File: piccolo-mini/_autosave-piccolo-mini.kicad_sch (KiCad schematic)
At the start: 13 parts, among them U1 ProMicro

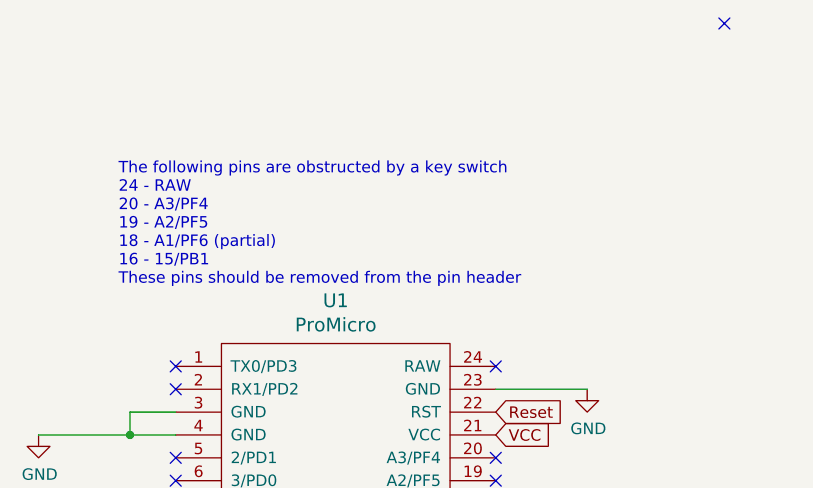
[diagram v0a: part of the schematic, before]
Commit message: Remove a few pro micro pins that get in the way
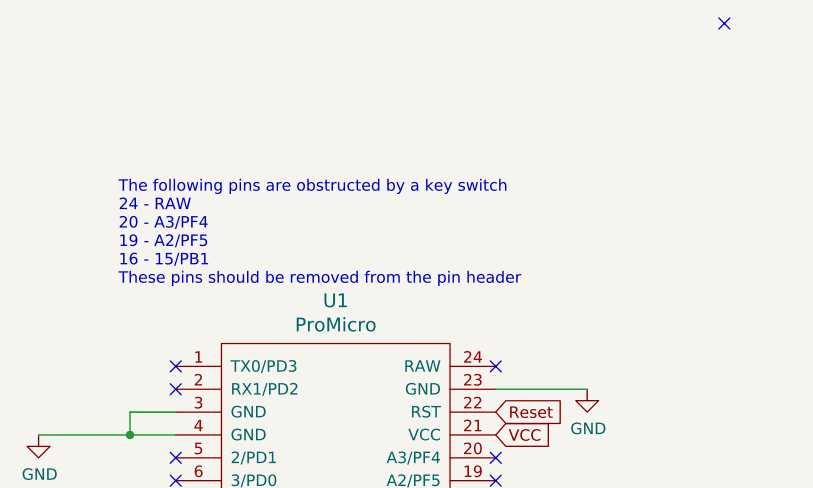
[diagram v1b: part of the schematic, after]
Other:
- note added: "The following pins are obstructed by a key switch 24 - RAW 20 - A3/PF4 19 - A2/PF5 16 - 15/PB1 These pins should be removed from the pin header"
- note removed: "The following pins are obstructed by a key switch 24 - RAW 20 - A3/PF4 19 - A2/PF5 18 - A1/PF6 (partial) 16 - 15/PB1 These pins should be removed from the pin header"
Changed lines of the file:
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@@
     (stroke (width 0) (type default) (color 0 0 0 0))
   )
-  (text "The following pins are obstructed by a key switch\n24 - RAW\n20 - A3/PF4\n19 - A2/PF5\n18 - A1/PF6 (partial)\n16 - 15/PB1\nThese pins should be removed from the pin header\n"
+  (text "The following pins are obstructed by a key switch\n24 - RAW\n20 - A3/PF4\n19 - A2/PF5\n16 - 15/PB1\nThese pins should be removed from the pin header\n"
     (at 35.56 33.02 0)
     (effects (font (size 1.27 1.27)) (justify left bottom))
